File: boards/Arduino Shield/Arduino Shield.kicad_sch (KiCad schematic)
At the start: 6 parts, among them J1 Screw_Terminal_01x09, J2 Screw_Terminal_01x09, J3 Screw_Terminal_01x09, J4 Screw_Terminal_01x09, J5 Screw_Terminal_01x09, J6 Screw_Terminal_01x09

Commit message: Shield Schematic
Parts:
- added J10: Screw_Terminal_01x04, symbol Connector:Screw_Terminal_01x04
- added J7, J8, J9: Screw_Terminal_01x09, symbol Connector:Screw_Terminal_01x09
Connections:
- net 5V: now also J10.1 (Pin_1), J10.2 (Pin_2)
- net GND: now also J10.3 (Pin_3), J10.4 (Pin_4)
- new net D27: J7.1 (Pin_1)
- new net D28: J7.2 (Pin_2)
- new net D29: J7.3 (Pin_3)
- new net D30: J7.4 (Pin_4)
- new net D31: J7.5 (Pin_5)
- new net D32: J7.6 (Pin_6)
- new net D33: J7.7 (Pin_7)
- new net D34: J7.8 (Pin_8)
- new net D35: J7.9 (Pin_9)
- new net D36: J8.1 (Pin_1)
- new net D37: J8.2 (Pin_2)
- new net D38: J8.3 (Pin_3)
- new net D39: J8.4 (Pin_4)
- new net D40: J8.5 (Pin_5)
- new net D41: J8.6 (Pin_6)
- new net D42: J8.7 (Pin_7)
- new net D43: J8.8 (Pin_8)
- new net D44: J8.9 (Pin_9)
- new net D45: J9.1 (Pin_1)
- new net D46: J9.2 (Pin_2)
- new net D47: J9.3 (Pin_3)
- new net D48: J9.4 (Pin_4)
- new net D49: J9.5 (Pin_5)
- new net D50: J9.6 (Pin_6)
- new net D51: J9.7 (Pin_7)
- new net D52: J9.8 (Pin_8)
- new net D53: J9.9 (Pin_9)

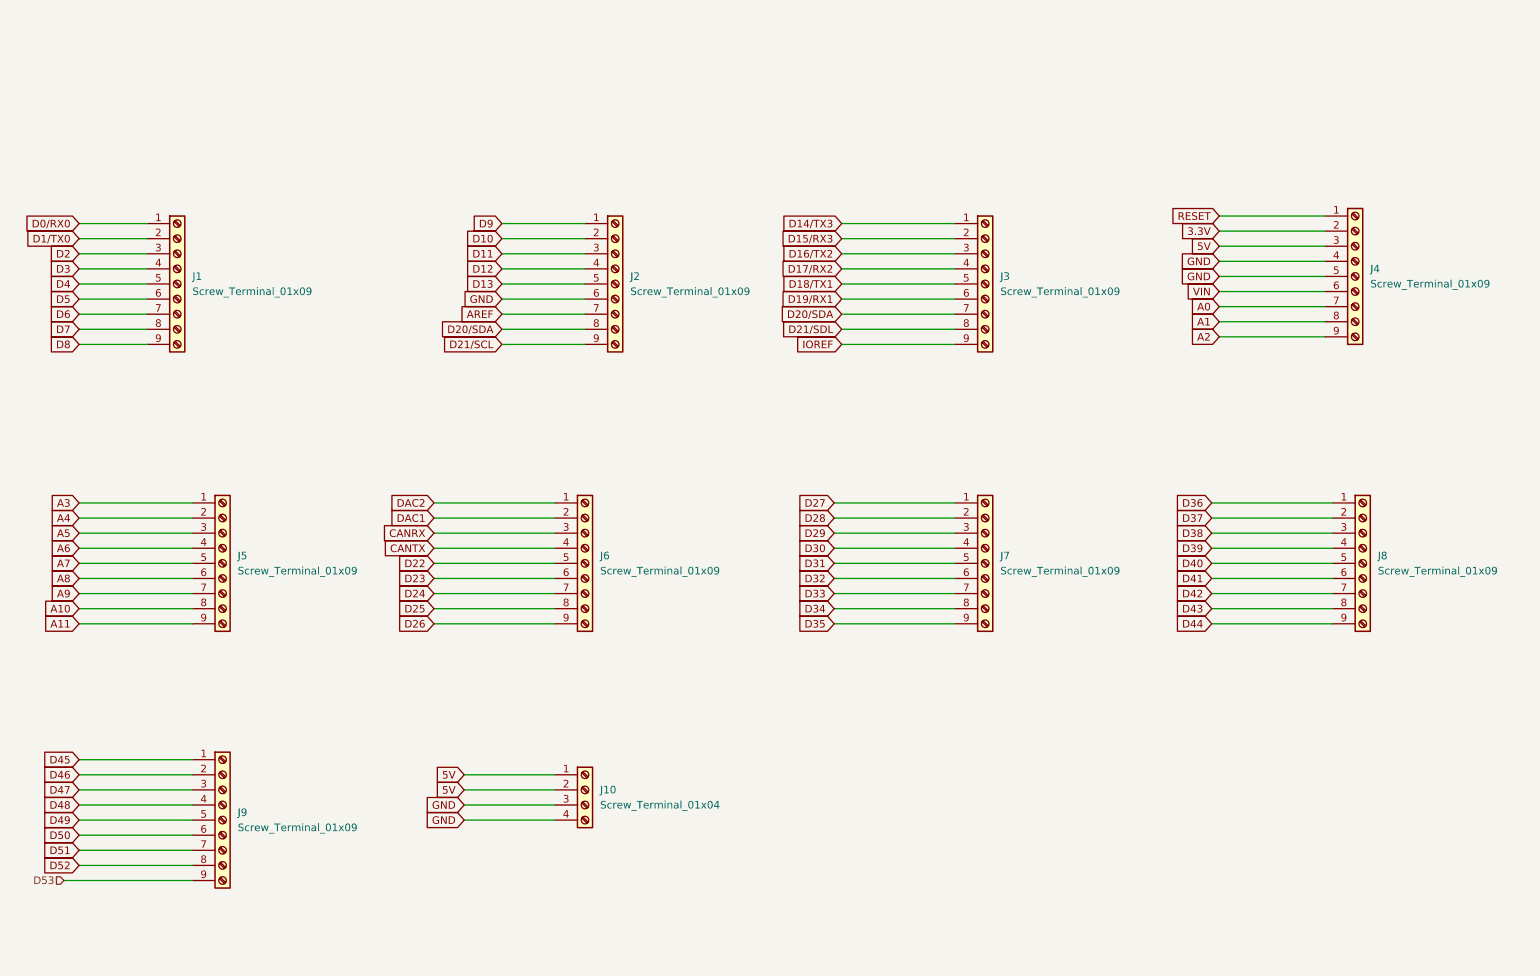
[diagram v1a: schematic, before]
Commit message: Updated Arduino Shield Schematic
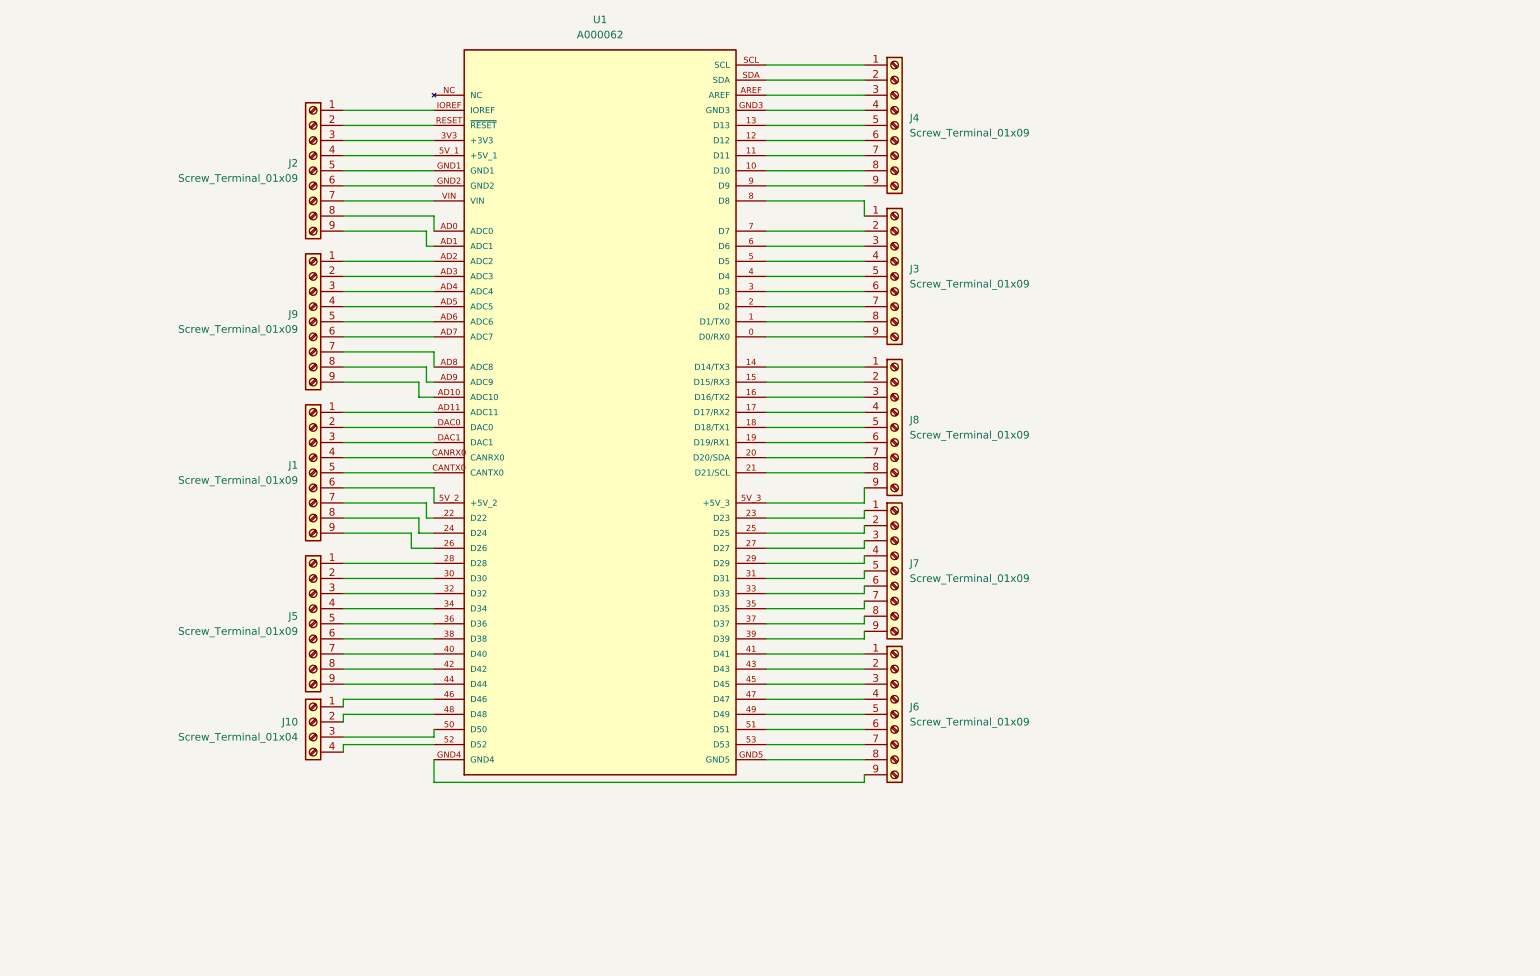
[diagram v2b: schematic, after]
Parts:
- added U1: A000062, A000062:MODULE_A000062, symbol A000062:A000062
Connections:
- net 3.3V: no longer names the net of J4.2 (Pin_2)
- net 3.3V: now also U1.SDA
- removed net 5V: J10.1 (Pin_1), J10.2 (Pin_2), J4.3 (Pin_3)
- net A0: no longer names the net of J4.7 (Pin_7)
- net A0: now also U1.11 (D11)
- net A1: no longer names the net of J4.8 (Pin_8)
- net A1: now also U1.10 (D10)
- net A10: no longer names the net of J5.8 (Pin_8)
- net A10: now also U1.42 (D42)
- net A11: no longer names the net of J5.9 (Pin_9)
- net A11: now also U1.44 (D44)
- net A2: no longer names the net of J4.9 (Pin_9)
- net A2: now also U1.9 (D9)
- net A3: no longer names the net of J5.1 (Pin_1)
- net A3: now also U1.28 (D28)
- net A4: no longer names the net of J5.2 (Pin_2)
- net A4: now also U1.30 (D30)
- net A5: no longer names the net of J5.3 (Pin_3)
- net A5: now also U1.32 (D32)
- net A6: no longer names the net of J5.4 (Pin_4)
- net A6: now also U1.34 (D34)
- net A7: no longer names the net of J5.5 (Pin_5)
- net A7: now also U1.36 (D36)
- net A8: no longer names the net of J5.6 (Pin_6)
- net A8: now also U1.38 (D38)
- net A9: no longer names the net of J5.7 (Pin_7)
- net A9: now also U1.40 (D40)
- net AREF: no longer names the net of J2.7 (Pin_7)
- net AREF: now also U1.VIN
- net CANRX: no longer names the net of J6.3 (Pin_3)
- net CANRX: now also U1.45 (D45)
- net CANTX: no longer names the net of J6.4 (Pin_4)
- net CANTX: now also U1.47 (D47)
- net D0/RX0: no longer names the net of J1.1 (Pin_1)
- net D0/RX0: now also U1.AD11 (ADC11)
- net D10: no longer names the net of J2.2 (Pin_2)
- net D10: now also U1.RESET (~{RESET})
- net D11: no longer names the net of J2.3 (Pin_3)
- net D11: now also U1.3V3 (+3V3)
- net D12: no longer names the net of J2.4 (Pin_4)
- net D12: now also U1.5V_1 (+5V_1)
- net D13: no longer names the net of J2.5 (Pin_5)
- net D13: now also U1.GND1
- net D14/TX3: no longer names the net of J3.1 (Pin_1)
- net D14/TX3: now also U1.8 (D8)
- net D15/RX3: no longer names the net of J3.2 (Pin_2)
- net D15/RX3: now also U1.7 (D7)
- net D16/TX2: no longer names the net of J3.3 (Pin_3)
- net D16/TX2: now also U1.6 (D6)
- net D17/RX2: no longer names the net of J3.4 (Pin_4)
- net D17/RX2: now also U1.5 (D5)
- net D18/TX1: no longer names the net of J3.5 (Pin_5)
- net D18/TX1: now also U1.4 (D4)
- net D19/RX1: no longer names the net of J3.6 (Pin_6)
- net D19/RX1: now also U1.3 (D3)
- net D1/TX0: no longer names the net of J1.2 (Pin_2)
- net D1/TX0: now also U1.DAC0
- net D2: no longer names the net of J1.3 (Pin_3)
- net D2: now also U1.DAC1
- net D20/SDA: no longer names the net of J2.8 (Pin_8)
- net D20/SDA: now also U1.AD0 (ADC0); no longer J3.7 (Pin_7)
- net D21/SCL: no longer names the net of J2.9 (Pin_9)
- net D21/SCL: now also U1.AD1 (ADC1)
- net D21/SDL: no longer names the net of J3.8 (Pin_8)
- net D21/SDL: now also U1.1 (D1/TX0)
- net D22: no longer names the net of J6.5 (Pin_5)
- net D22: now also U1.49 (D49)
- net D23: no longer names the net of J6.6 (Pin_6)
- net D23: now also U1.51 (D51)
- net D24: no longer names the net of J6.7 (Pin_7)
- net D24: now also U1.53 (D53)
- net D25: no longer names the net of J6.8 (Pin_8)
- net D25: now also U1.GND5
- net D26: no longer names the net of J6.9 (Pin_9)
- net D26: now also U1.GND4
- net D27: no longer names the net of J7.1 (Pin_1)
- net D27: now also U1.23 (D23)
- net D28: no longer names the net of J7.2 (Pin_2)
- net D28: now also U1.25 (D25)
- net D29: no longer names the net of J7.3 (Pin_3)
- net D29: now also U1.27 (D27)
- net D3: no longer names the net of J1.4 (Pin_4)
- net D3: now also U1.CANRX0
- net D30: no longer names the net of J7.4 (Pin_4)
- net D30: now also U1.29 (D29)
- net D31: no longer names the net of J7.5 (Pin_5)
- net D31: now also U1.31 (D31)
- net D32: no longer names the net of J7.6 (Pin_6)
- net D32: now also U1.33 (D33)
- net D33: no longer names the net of J7.7 (Pin_7)
- net D33: now also U1.35 (D35)
- net D34: no longer names the net of J7.8 (Pin_8)
- net D34: now also U1.37 (D37)
- net D35: no longer names the net of J7.9 (Pin_9)
- net D35: now also U1.39 (D39)
- net D36: no longer names the net of J8.1 (Pin_1)
- net D36: now also U1.14 (D14/TX3)
- net D37: no longer names the net of J8.2 (Pin_2)
- net D37: now also U1.15 (D15/RX3)
- net D38: no longer names the net of J8.3 (Pin_3)
- net D38: now also U1.16 (D16/TX2)
- net D39: no longer names the net of J8.4 (Pin_4)
- net D39: now also U1.17 (D17/RX2)
- net D4: no longer names the net of J1.5 (Pin_5)
- net D4: now also U1.CANTX0
- net D40: no longer names the net of J8.5 (Pin_5)
- net D40: now also U1.18 (D18/TX1)
- net D41: no longer names the net of J8.6 (Pin_6)
- net D41: now also U1.19 (D19/RX1)
- net D42: no longer names the net of J8.7 (Pin_7)
- net D42: now also U1.20 (D20/SDA)
- net D43: no longer names the net of J8.8 (Pin_8)
- net D43: now also U1.21 (D21/SCL)
- net D44: no longer names the net of J8.9 (Pin_9)
- net D44: now also U1.5V_3 (+5V_3)
- net D45: no longer names the net of J9.1 (Pin_1)
- net D45: now also U1.AD2 (ADC2)
- net D46: no longer names the net of J9.2 (Pin_2)
- net D46: now also U1.AD3 (ADC3)
- net D47: no longer names the net of J9.3 (Pin_3)
- net D47: now also U1.AD4 (ADC4)
- net D48: no longer names the net of J9.4 (Pin_4)
- net D48: now also U1.AD5 (ADC5)
- net D49: no longer names the net of J9.5 (Pin_5)
- net D49: now also U1.AD6 (ADC6)
- net D5: no longer names the net of J1.6 (Pin_6)
- net D5: now also U1.5V_2 (+5V_2)
- net D50: no longer names the net of J9.6 (Pin_6)
- net D50: now also U1.AD7 (ADC7)
- net D51: no longer names the net of J9.7 (Pin_7)
- net D51: now also U1.AD8 (ADC8)
- net D52: no longer names the net of J9.8 (Pin_8)
- net D52: now also U1.AD9 (ADC9)
- net D53: no longer names the net of J9.9 (Pin_9)
- net D53: now also U1.AD10 (ADC10)
- net D6: no longer names the net of J1.7 (Pin_7)
- net D6: now also U1.22 (D22)
- net D7: no longer names the net of J1.8 (Pin_8)
- net D7: now also U1.24 (D24)
- net D8: no longer names the net of J1.9 (Pin_9)
- net D8: now also U1.26 (D26)
- net D9: no longer names the net of J2.1 (Pin_1)
- net D9: now also U1.IOREF
- net DAC1: no longer names the net of J6.2 (Pin_2)
- net DAC1: now also U1.43 (D43)
- net DAC2: no longer names the net of J6.1 (Pin_1)
- net DAC2: now also U1.41 (D41)
- removed net GND: J10.3 (Pin_3), J10.4 (Pin_4), J2.6 (Pin_6), J4.4 (Pin_4), J4.5 (Pin_5)
- net IOREF: no longer names the net of J3.9 (Pin_9)
- net IOREF: now also U1.0 (D0/RX0)
- net RESET: no longer names the net of J4.1 (Pin_1)
- net RESET: now also U1.SCL
- net VIN: no longer names the net of J4.6 (Pin_6)
- net VIN: now also U1.12 (D12)
- new net: J2.6 (Pin_6), U1.GND2
- new net: J3.7 (Pin_7), U1.2 (D2)
- new net: J4.3 (Pin_3), U1.AREF
- new net: J4.4 (Pin_4), U1.GND3
- new net: J4.5 (Pin_5), U1.13 (D13)
- new net: J10.1 (Pin_1), U1.46 (D46)
- new net: J10.2 (Pin_2), U1.48 (D48)
- new net: J10.3 (Pin_3), U1.50 (D50)
- new net: J10.4 (Pin_4), U1.52 (D52)
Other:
- moved on the sheet: J1, J10, J2, J3, J4, J5, J6, J7, J8, J9

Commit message: updated arduino-shield footprint and rendered PCB
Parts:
- J1, J2, J3, J4, J5, J6, J7, J8, J9: footprint (none) -> TerminalBlock_4Ucon:TerminalBlock_4Ucon_1x09_P3.50mm_Horizontal
- J10: footprint (none) -> TerminalBlock_4Ucon:TerminalBlock_4Ucon_1x04_P3.50mm_Horizontal
- U1: footprint A000062:MODULE_A000062 -> Arduino_Due_Shield:Arduino_Due_Shield
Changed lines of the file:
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@@
       (effects (font (size 1.27 1.27)) (justify left))
     )
-    (property "Footprint" "" (at 68.58 43.18 0)
+    (property "Footprint" "TerminalBlock_4Ucon:TerminalBlock_4Ucon_1x09_P3.50mm_Horizontal" (at 68.58 43.18 0)
       (effects (font (size 1.27 1.27)) hide)
     )
@@
       (effects (font (size 1.27 1.27)) (justify left))
     )
-    (property "Footprint" "" (at 68.58 93.98 0)
+    (property "Footprint" "TerminalBlock_4Ucon:TerminalBlock_4Ucon_1x09_P3.50mm_Horizontal" (at 68.58 93.98 0)
       (effects (font (size 1.27 1.27)) hide)
     )
@@
       (effects (font (size 1.27 1.27)) (justify left))
     )
-    (property "Footprint" "" (at 166.37 60.96 0)
+    (property "Footprint" "TerminalBlock_4Ucon:TerminalBlock_4Ucon_1x09_P3.50mm_Horizontal" (at 166.37 60.96 0)
       (effects (font (size 1.27 1.27)) hide)
     )
@@
       (effects (font (size 1.27 1.27)) (justify left))
     )
-    (property "Footprint" "" (at 166.37 35.56 0)
+    (property "Footprint" "TerminalBlock_4Ucon:TerminalBlock_4Ucon_1x09_P3.50mm_Horizontal" (at 166.37 35.56 0)
       (effects (font (size 1.27 1.27)) hide)
     )
@@
       (effects (font (size 1.27 1.27)) (justify left))
     )
-    (property "Footprint" "" (at 166.37 110.49 0)
+    (property "Footprint" "TerminalBlock_4Ucon:TerminalBlock_4Ucon_1x09_P3.50mm_Horizontal" (at 166.37 110.49 0)
       (effects (font (size 1.27 1.27)) hide)
     )
@@
       (effects (font (size 1.27 1.27)) (justify left))
     )
-    (property "Footprint" "" (at 166.37 134.62 0)
+    (property "Footprint" "TerminalBlock_4Ucon:TerminalBlock_4Ucon_1x09_P3.50mm_Horizontal" (at 166.37 134.62 0)
       (effects (font (size 1.27 1.27)) hide)
     )
@@
       (effects (font (size 1.27 1.27)) (justify left))
     )
-    (property "Footprint" "" (at 68.58 135.89 0)
+    (property "Footprint" "TerminalBlock_4Ucon:TerminalBlock_4Ucon_1x04_P3.50mm_Horizontal" (at 68.58 135.89 0)
       (effects (font (size 1.27 1.27)) hide)
     )
@@
       (effects (font (size 1.27 1.27)) (justify left))
     )
-    (property "Footprint" "" (at 68.58 119.38 0)
+    (property "Footprint" "TerminalBlock_4Ucon:TerminalBlock_4Ucon_1x09_P3.50mm_Horizontal" (at 68.58 119.38 0)
       (effects (font (size 1.27 1.27)) hide)
     )
@@
       (effects (font (size 1.27 1.27)) (justify left))
     )
-    (property "Footprint" "" (at 68.58 68.58 0)
+    (property "Footprint" "TerminalBlock_4Ucon:TerminalBlock_4Ucon_1x09_P3.50mm_Horizontal" (at 68.58 68.58 0)
       (effects (font (size 1.27 1.27)) hide)
     )
@@
       (effects (font (size 1.27 1.27)))
     )
-    (property "Footprint" "A000062:MODULE_A000062" (at 116.84 83.82 0)
+    (property "Footprint" "Arduino_Due_Shield:Arduino_Due_Shield" (at 116.84 83.82 0)
       (effects (font (size 1.27 1.27)) (justify bottom) hide)
     )
@@
       (effects (font (size 1.27 1.27)) (justify left))
     )
-    (property "Footprint" "" (at 166.37 86.36 0)
-      (effects (font (size 1.27 1.27)) hide)
-    )
+    (property "Footprint" "TerminalBlock_4Ucon:TerminalBlock_4Ucon_1x09_P3.50mm_Horizontal" (at 166.37 86.36 0)
+      (effects (font (size 1.27 1.27)) hide)
+    )
